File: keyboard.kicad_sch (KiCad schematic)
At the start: 58 parts, among them SW1 SW_SPDT, SW10 SW_Push, SW11 RotaryEncoder_Switch, SW2 SW_Push, SW3 SW_Push, SW4 SW_Push, SW5 SW_Push, SW6 SW_Push, SW7 SW_Push, SW8 SW_Push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

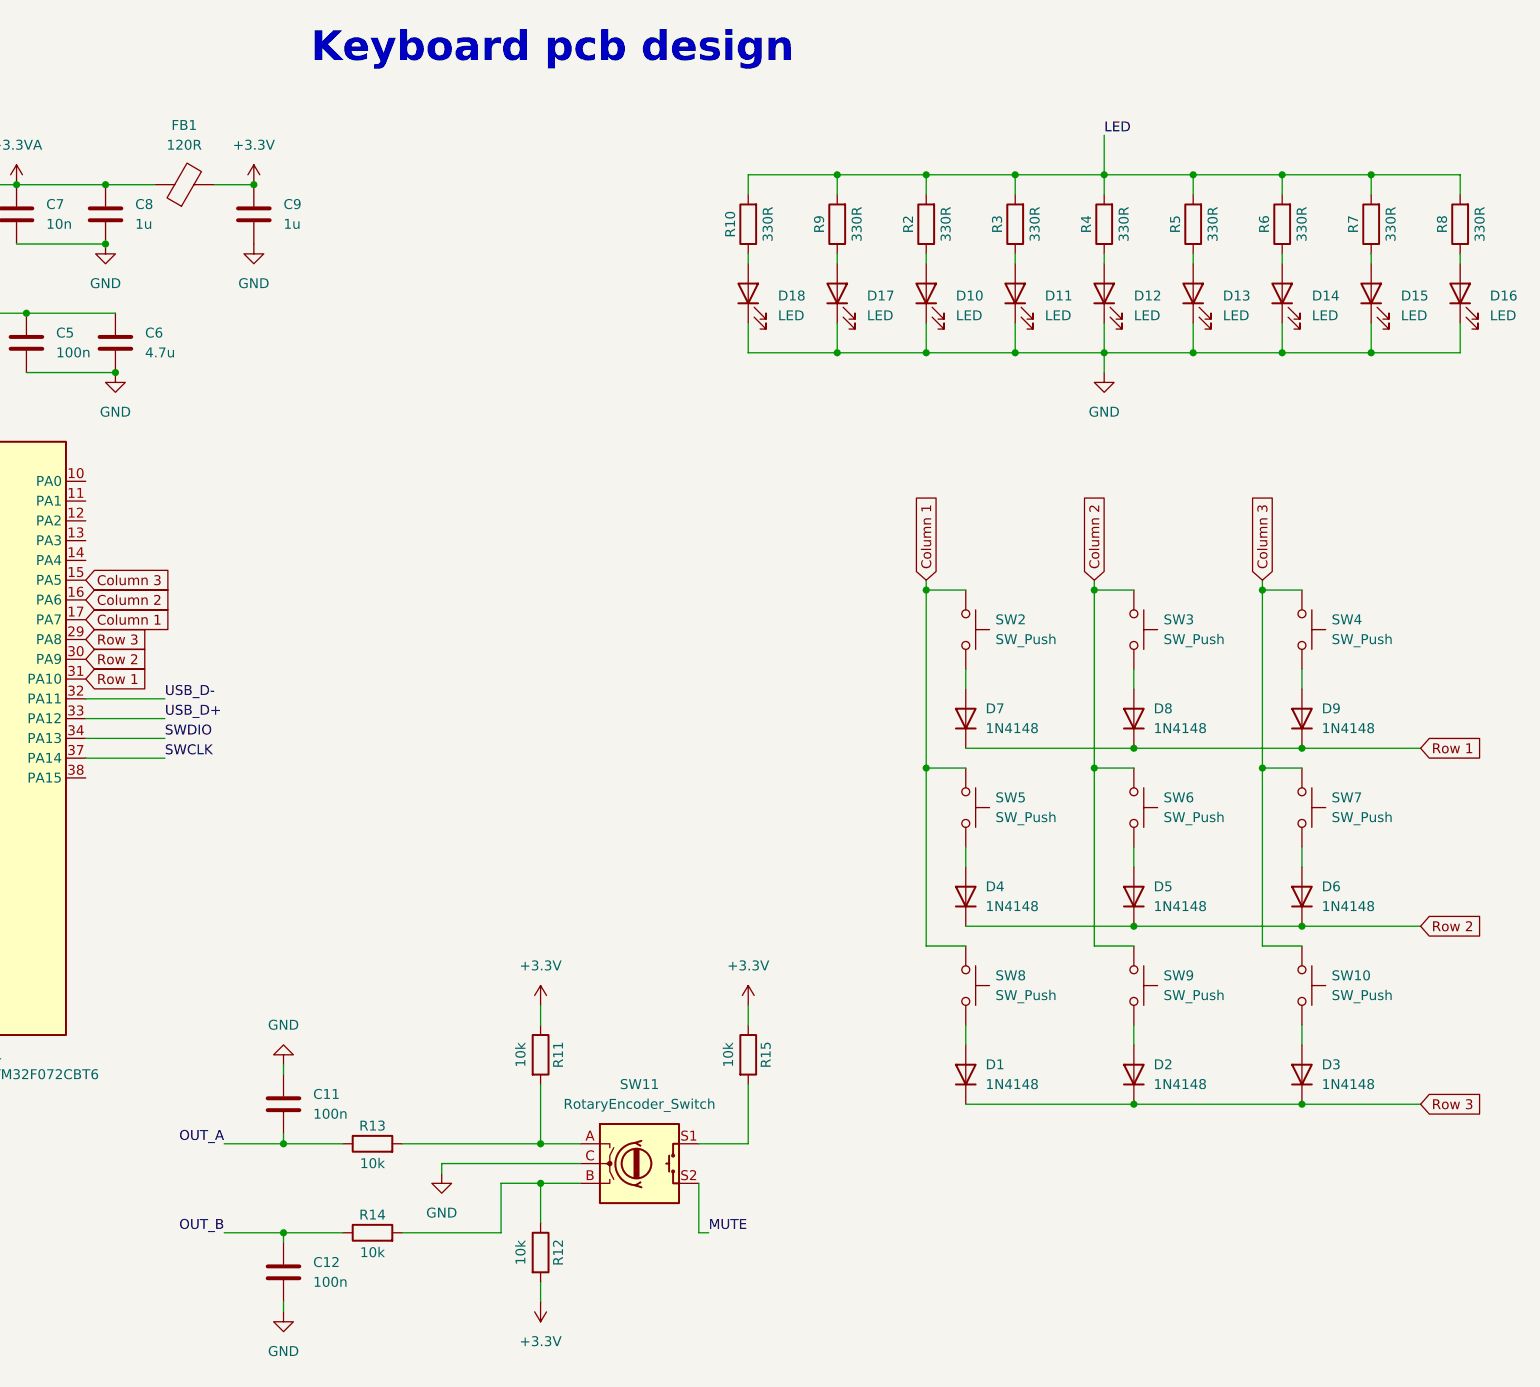
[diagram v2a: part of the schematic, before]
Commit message: Fix key leds
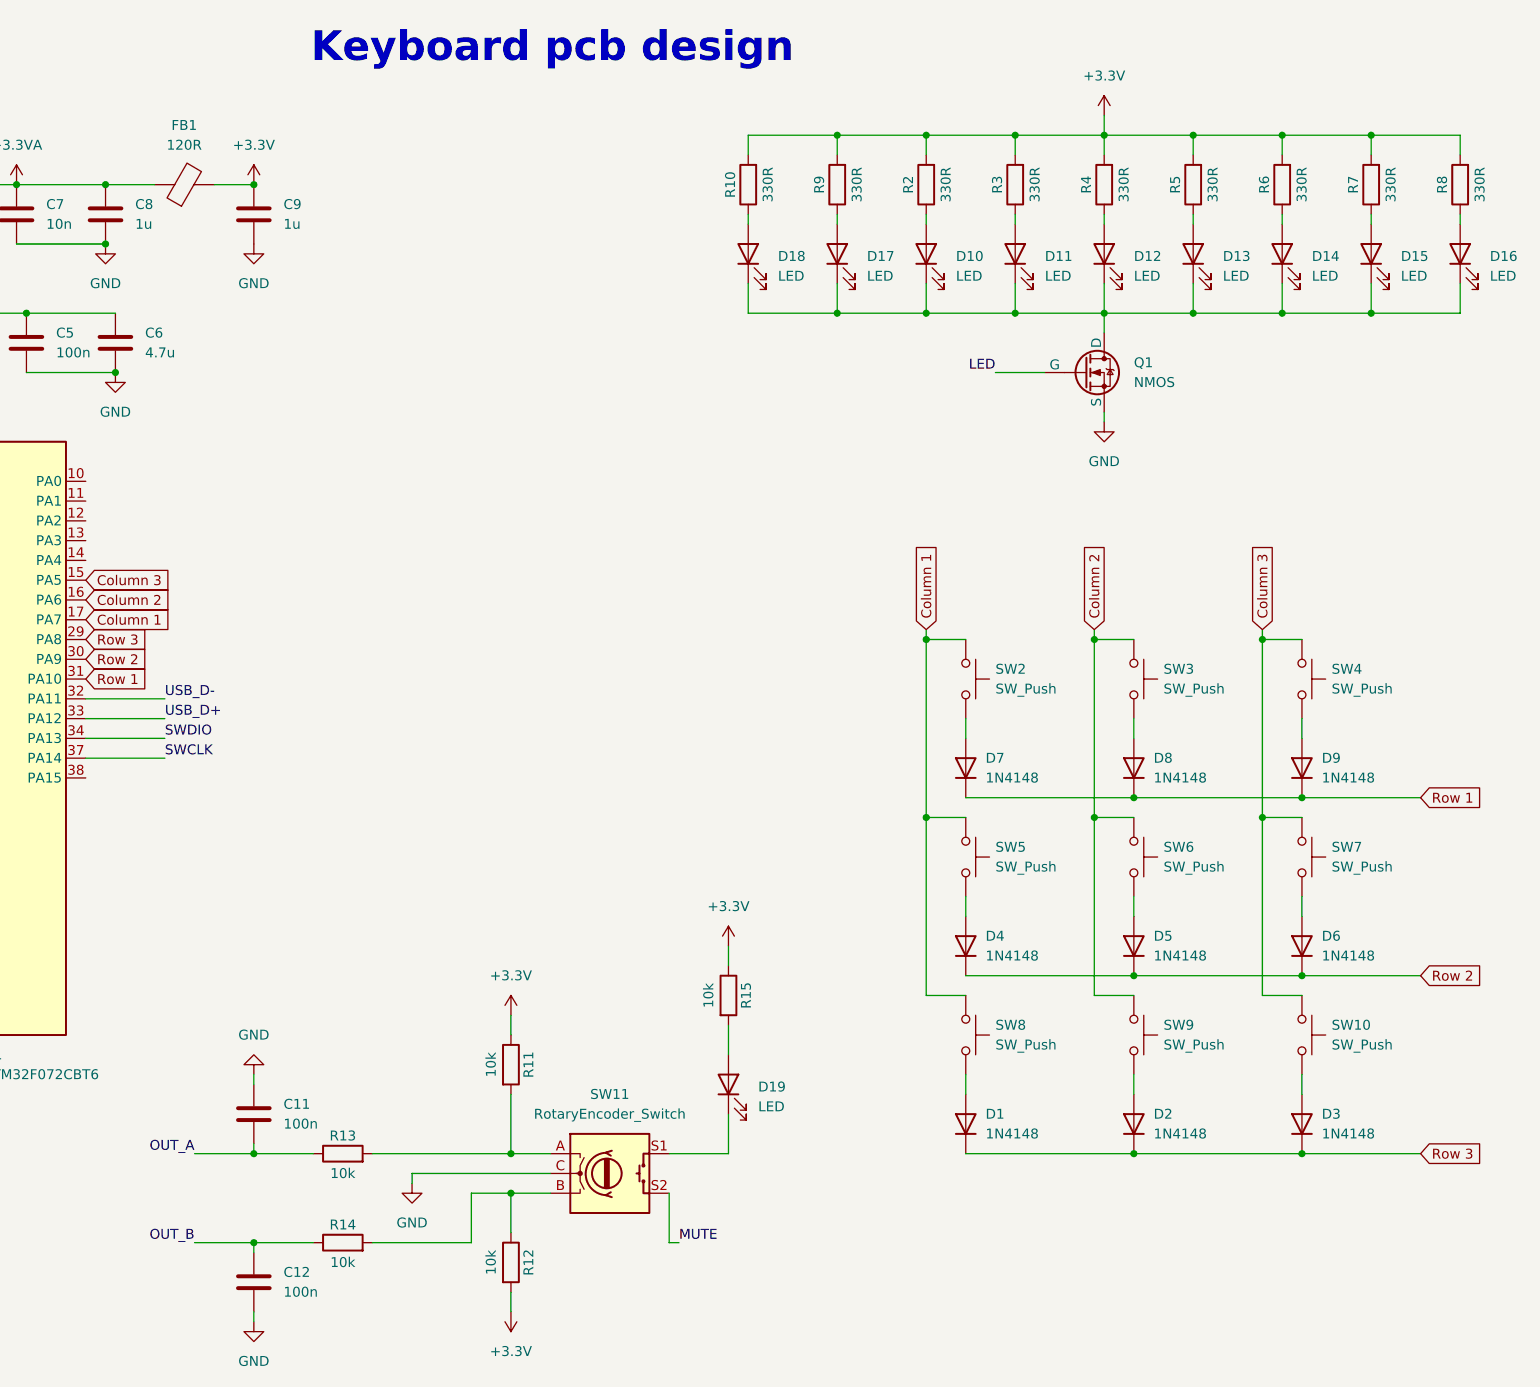
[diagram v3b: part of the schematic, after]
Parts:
- added D19: LED, symbol Device:LED
- added Q1: NMOS, symbol Simulation_SPICE:NMOS
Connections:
- net +3.3V: now also R10.2, R2.2, R3.2, R4.2, R5.2, R6.2, R7.2, R8.2, R9.2
- net GND: now also Q1.3 (S); no longer D10.1 (K), D11.1 (K), D12.1 (K), D13.1 (K), D14.1 (K), D15.1 (K), D16.1 (K), D17.1 (K), D18.1 (K)
- net LED: now also Q1.2 (G); no longer R10.2, R2.2, R3.2, R4.2, R5.2, R6.2, R7.2, R8.2, R9.2
- net at SW11.S1: now also D19.1 (K); no longer R15.2
- new net: D10.1 (K), D11.1 (K), D12.1 (K), D13.1 (K), D14.1 (K), D15.1 (K), D16.1 (K), D17.1 (K), D18.1 (K), Q1.1 (D)
- new net: D19.2 (A), R15.2
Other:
- moved on the sheet: C11, C12, D1, D10, D11, D12, D13, D14, D15, D16, D17, D18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

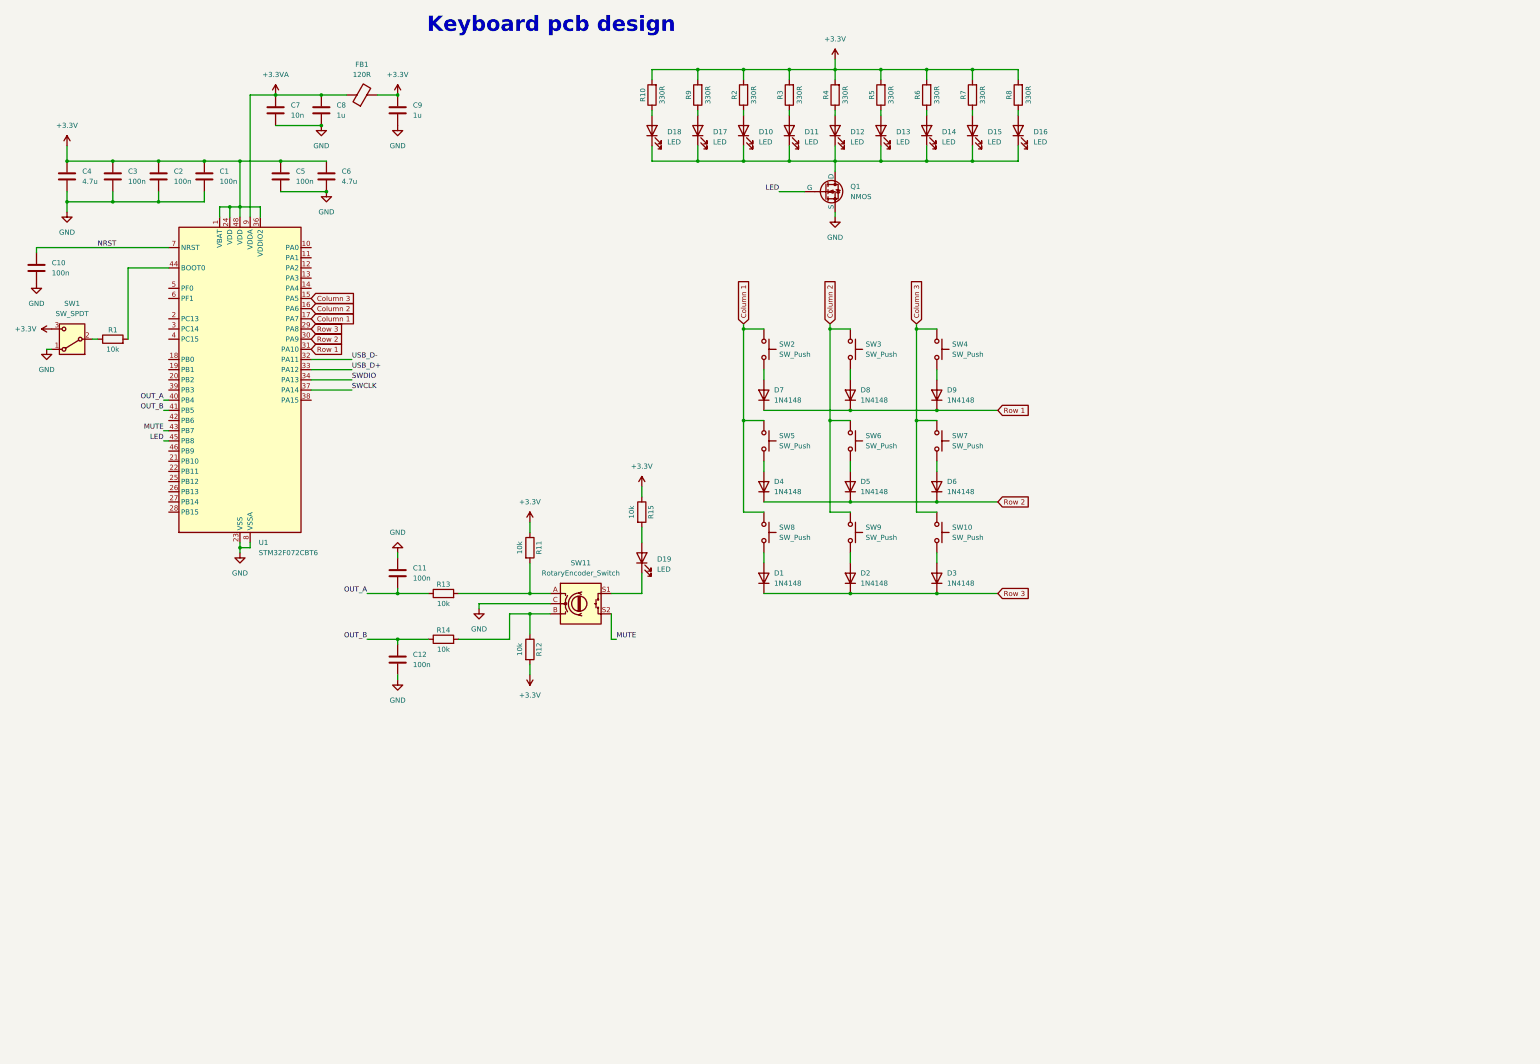
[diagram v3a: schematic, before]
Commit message: Added usb-c power supply
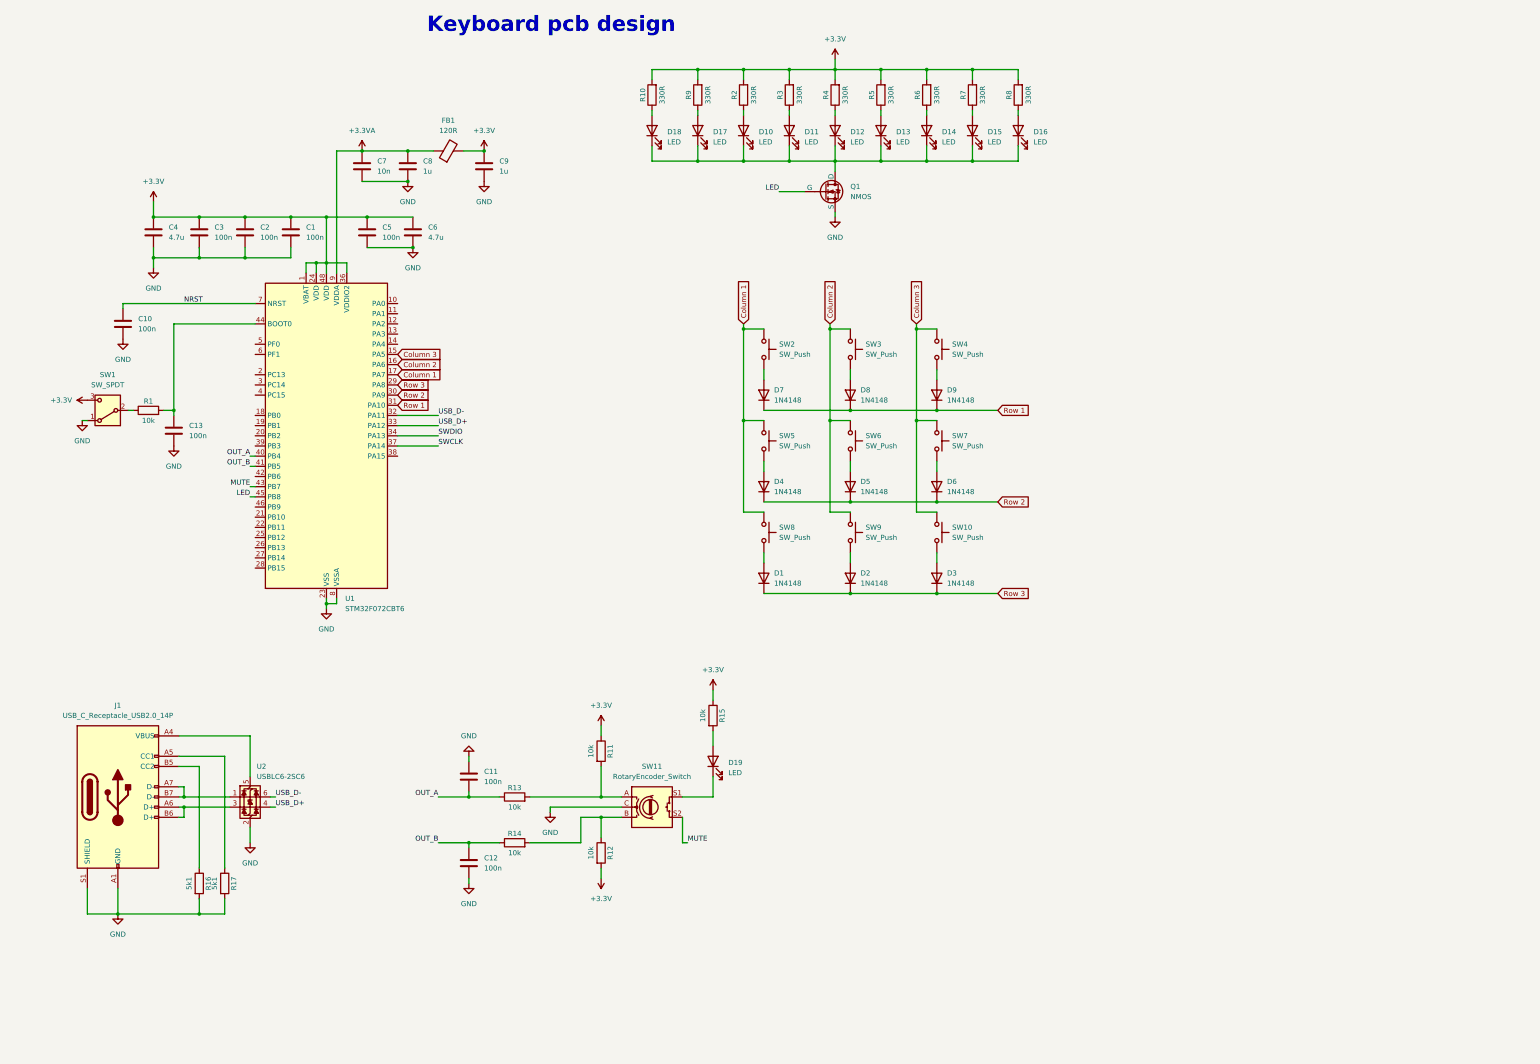
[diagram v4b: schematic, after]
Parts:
- added C13: 100n, symbol Device:C
- added J1: USB_C_Receptacle_USB2.0_14P, symbol Connector:USB_C_Receptacle_USB2.0_14P
- added R16, R17: 5k1, symbol Device:R
- added U2: USBLC6-2SC6, Package_TO_SOT_SMD:SOT-23-6, symbol Power_Protection:USBLC6-2SC6
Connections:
- net GND: now also C13.2, J1.A1 (GND), J1.A12 (GND), J1.B1 (GND), J1.B12 (GND), J1.S1 (SHIELD), R16.2, R17.2, U2.2 (GND)
- net USB_D+: now also U2.4 (I/O2)
- net USB_D-: now also U2.6 (I/O1)
- net at R1.2, U1.44 (BOOT0): now also C13.1
- new net: J1.A7 (D-), J1.B7 (D-), U2.1 (I/O1)
- new net: J1.A6 (D+), J1.B6 (D+), U2.3 (I/O2)
- new net: J1.A4 (VBUS), J1.A9 (VBUS), J1.B4 (VBUS), J1.B9 (VBUS), U2.5 (VBUS)
- new net: J1.A5 (CC1), R17.1
- new net: J1.B5 (CC2), R16.1
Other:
- moved on the sheet: C1, C10, C11, C12, C2, C3, C4, C5, C6, C7, C8, C9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

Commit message: Added LDO regulator
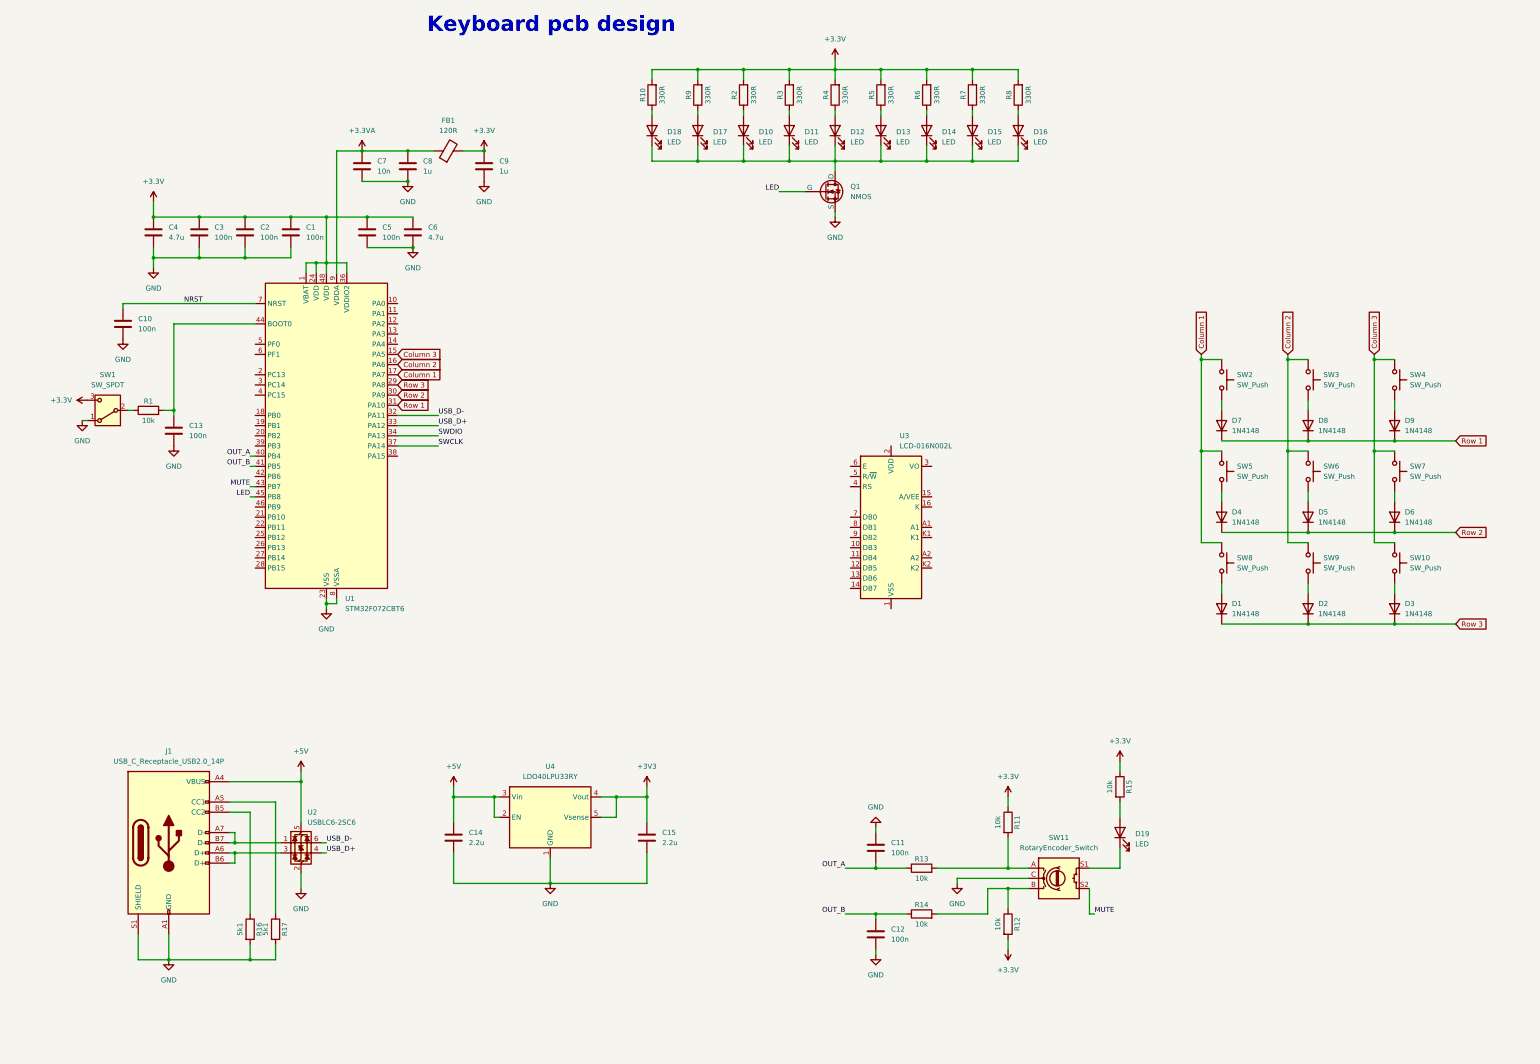
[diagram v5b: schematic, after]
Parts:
- added C14, C15: 2.2u, symbol Device:C
- added U3: LCD-016N002L, Display:LCD-016N002L, symbol Display_Character:LCD-016N002L
- added U4: LDO40LPU33RY, Package_DFN_QFN:DFN-6-1EP_3x3mm_P0.95mm_EP1.7x2.6mm, symbol Regulator_Linear:LDO40LPU33RY
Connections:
- net GND: now also C14.2, C15.2, U4.1 (GND), U4.7 (GND)
- net +5V: now reaches J1.A4 (VBUS), J1.A9 (VBUS), J1.B4 (VBUS), J1.B9 (VBUS), U2.5 (VBUS)
- net +5V: now also C14.1, U4.2 (EN), U4.3 (Vin)
- new net +3V3: C15.1, U4.4 (Vout), U4.5 (Vsense)
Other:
- moved on the sheet: C11, C12, D1, D19, D2, D3, D4, D5, D6, D7, D8, D9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

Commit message: Update BOOT0 pin
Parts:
- removed C13: 100n, symbol Device:C
- removed SW1: SW_SPDT, symbol Switch:SW_SPDT
- added D20: LED, symbol Device:LED
- added SW1: SW_Push, symbol Switch:SW_Push
- C14, C15: value 2.2u -> 4.7u
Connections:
- net +3.3V: now also SW1.1
- net +5V: now also D20.2 (A); no longer U4.2 (EN), U4.3 (Vin)
- net GND: now also R1.1
- net at R1.2, U1.44 (BOOT0): now also SW1.2
- new net: D20.1 (K), U4.2 (EN), U4.3 (Vin)
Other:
- moved on the sheet: D10, D11, D12, D13, D14, D15, D16, D17, D18, Q1, R1, R10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
